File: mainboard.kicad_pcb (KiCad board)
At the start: 4 copper layers, 150 x 70 mm, 101 parts, among them J1 HX711, J10 MainPump, J11 WaterLevelSensor, J12 AuxPump, J13 OneWireTemp, J14 OneWireTemp, J15 FlowSensor, J16 USB_C_Receptacle_USB2.0_16P, J17 Conn_01x14_MountingPin, J18 Conn_01x14_MountingPin, J2 Servo, J20 DC 12V IN, J3 Valve1, J4 Valve2, J5 Valve3, J6 Valve4, J7 Valve5, J8 Valve6, J9 Valve7, Q1 IRLML2502, Q11 IRLML2502, Q2 IRLML2502, Q3 IRLML2502, Q4 IRLML2502, Q5 IRLML2502, Q6 IRLML2502, Q7 IRLML2502, Q8 IRLML2502, U1 AP62150WU, U2 DRV8870DDAR, U3 TLV75533PDBV, U4 USBLC6-2SC6, U5 ESP32-S3-WROOM-1

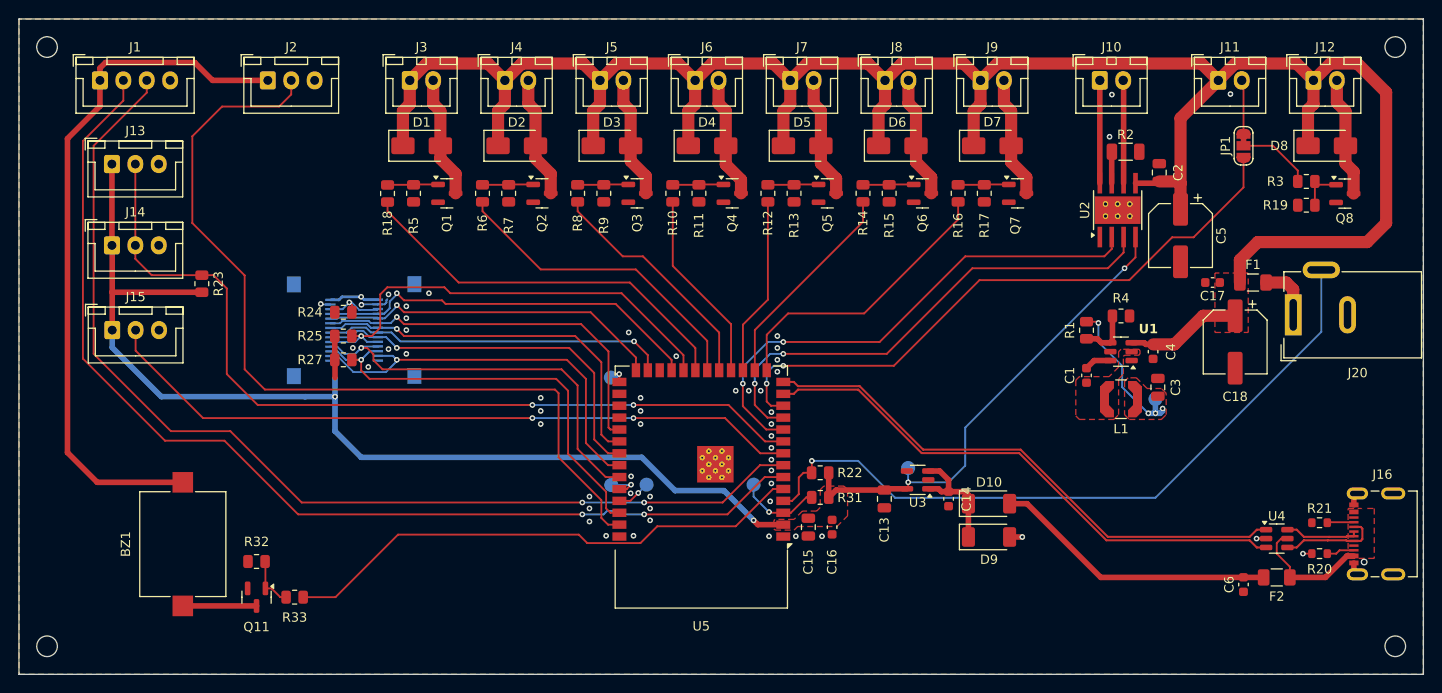
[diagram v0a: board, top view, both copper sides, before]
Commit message: Reannotate geographically by layout
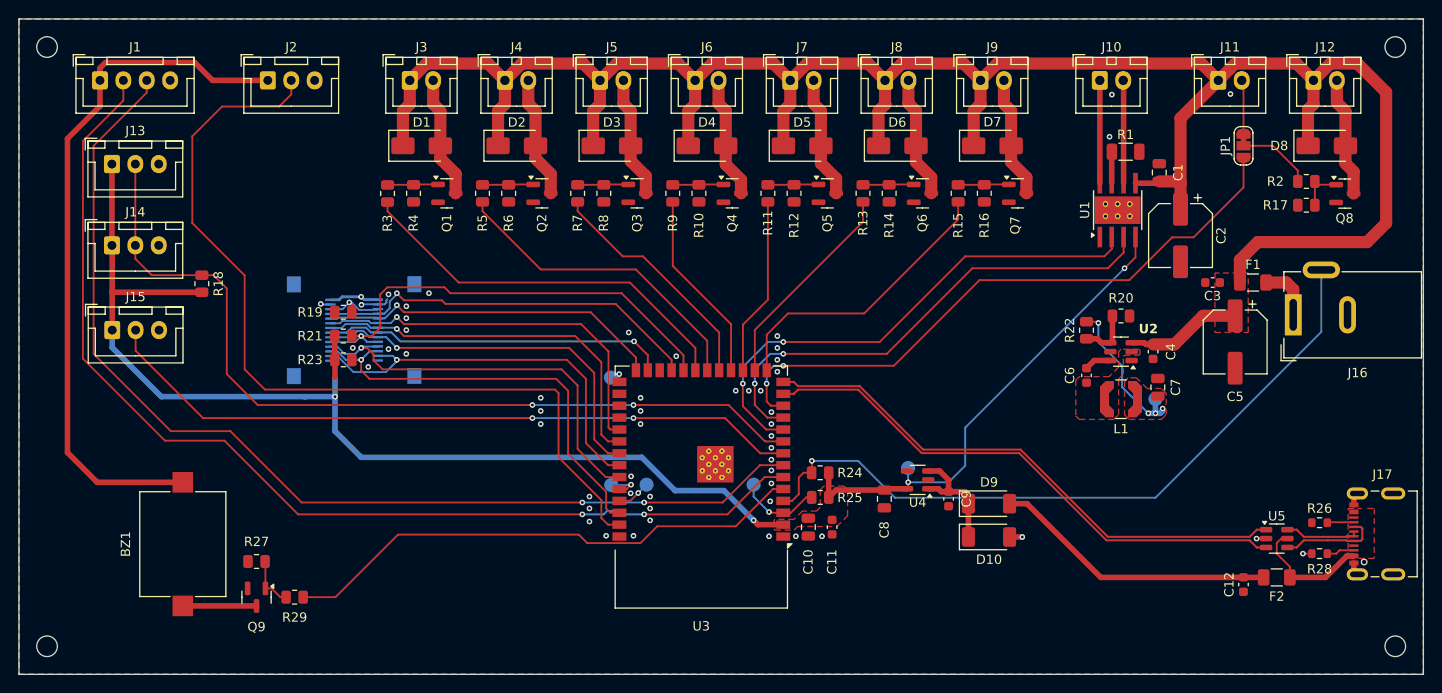
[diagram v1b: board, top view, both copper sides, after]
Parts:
- renumbered C2 to C1, C15 to C10, C16 to C11, C6 to C12, C5 to C2, C17 to C3, C18 to C5, C1 to C6, C3 to C7, C13 to C8, C14 to C9, D9 to D10, D10 to D9, J20 to J16, J16 to J17, J17 to J18, J18 to J19, Q11 to Q9, R2 to R1, R11 to R10, R12 to R11, R13 to R12, R14 to R13, R15 to R14, R16 to R15, R17 to R16, R19 to R17, R23 to R18, R24 to R19, R3 to R2, R4 to R20, R25 to R21, R1 to R22, R27 to R23, R22 to R24, R31 to R25, R21 to R26, R32 to R27, R20 to R28, R33 to R29, R18 to R3, R5 to R4, R6 to R5, R7 to R6, R8 to R7, R9 to R8, R10 to R9, TP6 to TP1, TP1 to TP2, TP10 to TP3, TP7 to TP4, TP8 to TP5, TP9 to TP6, U2 to U1, U1 to U2, U5 to U3, U3 to U4, U4 to U5

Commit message: Final checks and cleanup
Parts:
- moved G*** 14.2 mm to (74.3, 95.0)
- moved G*** 7.29 mm to (61.3, 95.0)
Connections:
- J11 pad 1: +12V -> +3.3V
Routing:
- net +3.3V: track 169.7 -> 190.7 mm
- net +5V: track 98.4 -> 78.1 mm
- net /MCU/SERVO_CTRL: track 93.2 -> 77.3 mm
- net +12V: track 242.7 -> 236.6 mm
- net /MCU/AUX_PUMP_CTRL: track 67.3 -> 68.4 mm
- net GND: vias 52 -> 55
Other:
- board text added: "JLCJLCJLCJLC"
- board text added: "inspired by kauzerei https://kauzerei.github.io/openautolab"
- board text removed: "Power"
- board text removed: "idea by kauzerei https://kauzerei.github.io/openautolab"

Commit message: Fix revision
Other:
- board text added: "openautolab alternative mainboard rev. 1"
- board text removed: "openautolab mainboard rev.2"

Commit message: Add GND via stitching
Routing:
- net GND: vias 55 -> 275

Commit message: - Start Rev 2 - Add 5k1 resistor (R30) parallel to piezo (BZ1) - Remove redundant 5V wire from bottom at buck converter (U2)
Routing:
- net +5V: track 78.1 -> 66.2 mm
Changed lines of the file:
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@@
   (via (at 82.55 58.674) (size 0.6) (drill 0.3) (layers "F.Cu" "B.Cu") (net 15))
   (segment (start 80.518 58.674) (end 80.19057 59.00143) (width 0.3) (layer "B.Cu") (net 15))
-  (segment (start 163.83 68.326) (end 166.624 71.12) (width 0.2) (layer "B.Cu") (net 15))
   (segment (start 82.55 58.674) (end 80.518 58.674) (width 0.3) (layer "B.Cu") (net 15))
   (segment (start 167.386 71.12) (end 166.624 71.12) (width 0.6) (layer "B.Cu") (net 15))
@@
   (segment (start 80.19057 59.00143) (end 79.26357 59.00143) (width 0.3) (layer "B.Cu") (net 15))
   (segment (start 84.335 58.98) (end 82.856 58.98) (width 0.3) (layer "B.Cu") (net 15))
-  (segment (start 161.29 63.5) (end 163.83 66.04) (width 0.2) (layer "B.Cu") (net 15))
   (segment (start 168.148 70.866) (end 168.148 70.612) (width 0.6) (layer "B.Cu") (net 15))
   (segment (start 167.386 71.12) (end 167.894 71.12) (width 0.6) (layer "B.Cu") (net 15))
-  (segment (start 163.83 66.04) (end 163.83 68.326) (width 0.2) (layer "B.Cu") (net 15))
   (segment (start 82.856 58.98) (end 82.55 58.674) (width 0.3) (layer "B.Cu") (net 15))
-  (segment (start 161.29 61.468) (end 161.29 63.5) (width 0.2) (layer "B.Cu") (net 15))
   (segment (start 167.386 69.596) (end 167.386 71.12) (width 0.6) (layer "B.Cu") (net 15))
   (segment (start 110.13 83.010001) (end 108.918001 83.010001) (width 0.2) (layer "F.Cu") (net 16))
